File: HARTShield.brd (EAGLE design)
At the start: 61.9 x 66 mm, 31 parts, among them Y1 3M6864

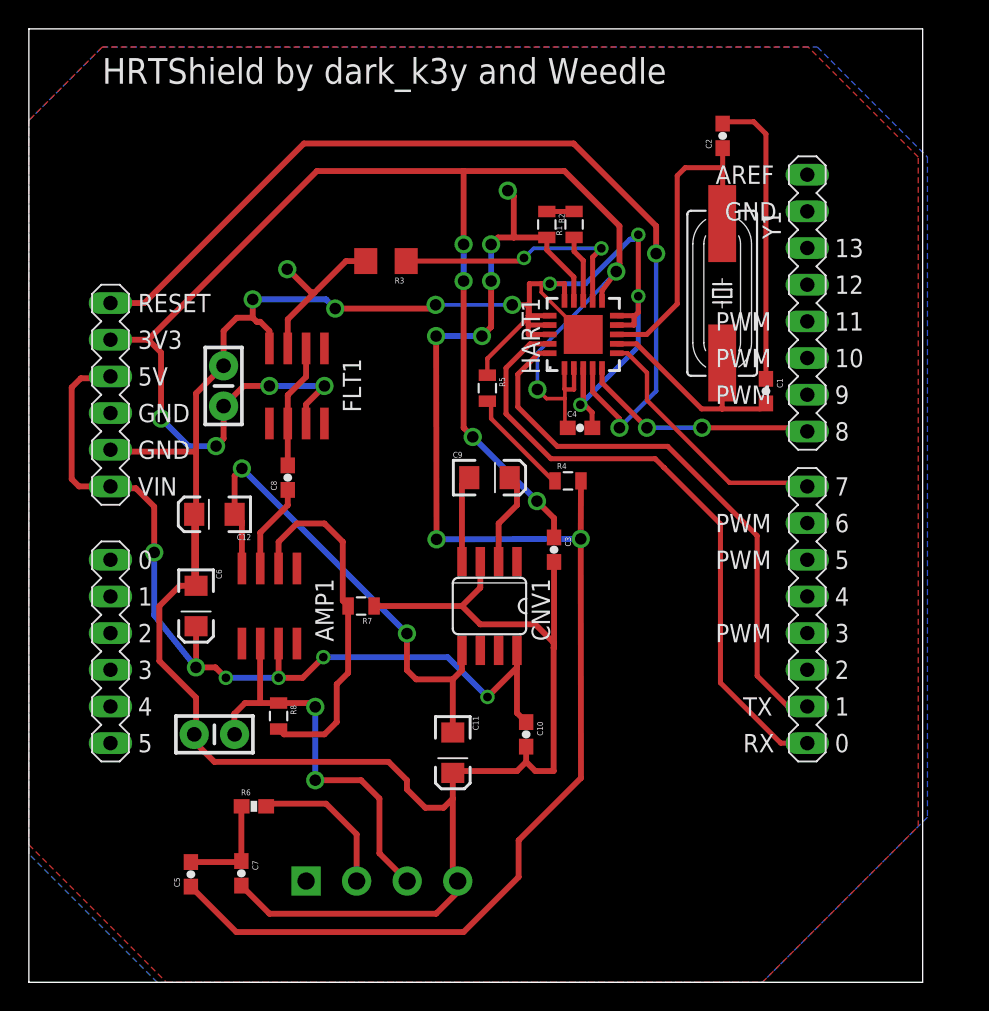
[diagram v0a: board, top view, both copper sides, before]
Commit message: Minor fixes on partlist.
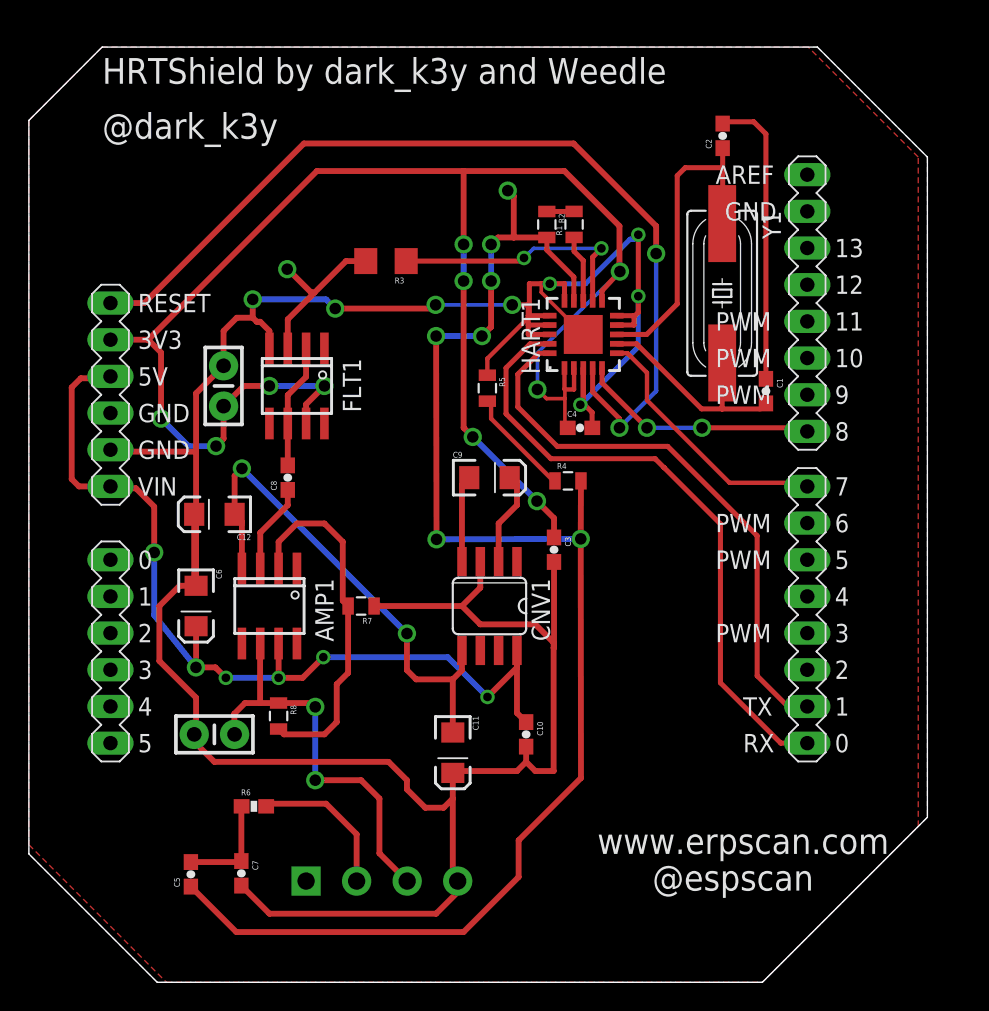
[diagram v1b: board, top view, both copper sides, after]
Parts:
- AMP1: value OP177GS -> OP37GS
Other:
- board size 61.9 x 66 mm -> 62.2 x 64.8 mm
- board text added: "@dark_k3y"
- board text added: "@espscan"
- board text added: "www.erpscan.com"
- board text removed: "GND"
- board text removed: "HI"
- board text removed: "HO"
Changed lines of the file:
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@@
 <layer number="25" name="tNames" color="7" fill="1" visible="yes" active="yes"/>
 <layer number="26" name="bNames" color="7" fill="1" visible="yes" active="yes"/>
-<layer number="27" name="tValues" color="7" fill="1" visible="no" active="yes"/>
-<layer number="28" name="bValues" color="7" fill="1" visible="no" active="yes"/>
+<layer number="27" name="tValues" color="7" fill="1" visible="yes" active="yes"/>
+<layer number="28" name="bValues" color="7" fill="1" visible="yes" active="yes"/>
 <layer number="29" name="tStop" color="7" fill="3" visible="no" active="yes"/>
 <layer number="30" name="bStop" color="7" fill="6" visible="no" active="yes"/>
@@
 <board>
 <plain>
-<wire x1="21.59" y1="6.35" x2="83.49" y2="6.35" width="0" layer="20"/>
-<wire x1="83.49" y1="6.35" x2="83.49" y2="72.38" width="0" layer="20"/>
-<wire x1="83.49" y1="72.38" x2="21.59" y2="72.38" width="0" layer="20"/>
-<wire x1="21.59" y1="72.38" x2="21.59" y2="6.35" width="0" layer="20"/>
+<wire x1="30.48" y1="6.35" x2="72.39" y2="6.35" width="0" layer="20"/>
+<wire x1="72.39" y1="6.35" x2="83.82" y2="17.78" width="0" layer="20"/>
+<wire x1="83.82" y1="17.78" x2="83.82" y2="63.5" width="0" layer="20"/>
+<wire x1="83.82" y1="63.5" x2="76.2" y2="71.12" width="0" layer="20"/>
+<wire x1="26.67" y1="71.12" x2="76.2" y2="71.12" width="0" layer="20"/>
+<wire x1="21.59" y1="66.04" x2="21.59" y2="15.24" width="0" layer="20"/>
+<wire x1="21.59" y1="15.24" x2="30.48" y2="6.35" width="0" layer="20"/>
 <circle x="27.241" y="35.612" radius="0.35" width="0.4" layer="116"/>
 <circle x="75.501" y="22.912" radius="0.35" width="0.4" layer="116"/>
@@
 <circle x="36.344" y="41.935" radius="0.3" width="0.3" layer="116"/>
 <text x="26.67" y="68.58" size="1.778" layer="25" font="vector" ratio="15">HRTShield by dark_k3y and Weedle</text>
-<text x="44.45" y="7.62" size="1.778" layer="26" font="vector" ratio="15" rot="MR0">HI</text>
-<text x="49.53" y="7.62" size="1.778" layer="26" font="vector" ratio="15" rot="MR0">HO</text>
-<text x="55.88" y="7.62" size="1.778" layer="26" font="vector" ratio="15" rot="MR0">GND</text>
+<text x="26.67" y="64.77" size="1.778" layer="25" ratio="15">@dark_k3y</text>
+<text x="64.77" y="12.7" size="1.778" layer="25" ratio="15">@espscan</text>
+<text x="60.96" y="15.24" size="1.778" layer="25" ratio="15">www.erpscan.com</text>
+<wire x1="26.66" y1="71.12" x2="21.59" y2="66.04" width="0" layer="20"/>
 </plain>
 <attributes>
@@
 </class>
 </classes>
-<designrules name="default">
-<description language="de">&lt;b&gt;EAGLE Design Rules&lt;/b&gt;
+<designrules name="DFRobot_Eagle_Rule_v0.4">
+<description language="en">
+&lt;b&gt;EAGLE Design Rules&lt;/b&gt;
 &lt;p&gt;
-Die Standard-Design-Rules sind so gewählt, dass sie für
-die meisten Anwendungen passen. Sollte ihre Platine
-besondere Anforderungen haben, treffen Sie die erforderlichen
-Einstellungen hier und speichern die Design Rules unter
-einem neuen Namen ab.</description>
-<description language="en">&lt;b&gt;EAGLE Design Rules&lt;/b&gt;
+The default Design Rules have been set to cover
+a wide range of applications. Your particular design
+may have different requirements, so please make the
+necessary adjustments and save your customized
+design rules under a new name.
+</description>
+<description language="it">
+&lt;b&gt;EAGLE Design Rules&lt;/b&gt;
 &lt;p&gt;
 The default Design Rules have been set to cover
@@
 <param name="mtCopper" value="0.035mm 0.035mm 0.035mm 0.035mm 0.035mm 0.035mm 0.035mm 0.035mm 0.035mm 0.035mm 0.035mm 0.035mm 0.035mm 0.035mm 0.035mm 0.035mm"/>
 <param name="mtIsolate" value="1.5mm 0.15mm 0.2mm 0.15mm 0.2mm 0.15mm 0.2mm 0.15mm 0.2mm 0.15mm 0.2mm 0.15mm 0.2mm 0.15mm 0.2mm"/>
-<param name="mdWireWire" value="8mil"/>
-<param name="mdWirePad" value="8mil"/>
-<param name="mdWireVia" value="8mil"/>
-<param name="mdPadPad" value="8mil"/>
-<param name="mdPadVia" value="8mil"/>
-<param name="mdViaVia" value="8mil"/>
-<param name="mdSmdPad" value="8mil"/>
-<param name="mdSmdVia" value="8mil"/>
-<param name="mdSmdSmd" value="8mil"/>
+<param name="mdWireWire" value="6mil"/>
+<param name="mdWirePad" value="6mil"/>
+<param name="mdWireVia" value="6mil"/>
+<param name="mdPadPad" value="6mil"/>
+<param name="mdPadVia" value="6mil"/>
+<param name="mdViaVia" value="6mil"/>
+<param name="mdSmdPad" value="0mil"/>
+<param name="mdSmdVia" value="0mil"/>
+<param name="mdSmdSmd" value="0mil"/>
 <param name="mdViaViaSameLayer" value="8mil"/>
 <param name="mnLayersViaInSmd" value="2"/>
-<param name="mdCopperDimension" value="40mil"/>
-<param name="mdDrill" value="8mil"/>
+<param name="mdCopperDimension" value="10mil"/>
+<param name="mdDrill" value="10mil"/>
 <param name="mdSmdStop" value="0mil"/>
-<param name="msWidth" value="10mil"/>
-<param name="msDrill" value="24mil"/>
-<param name="msMicroVia" value="9.99mm"/>
+<param name="msWidth" value="6mil"/>
+<param name="msDrill" value="12mil"/>
+<param name="msMicroVia" value="12mil"/>
 <param name="msBlindViaRatio" value="0.5"/>
 <param name="rvPadTop" value="0.25"/>
@@
 <param name="rvMicroViaOuter" value="0.25"/>
 <param name="rvMicroViaInner" value="0.25"/>
-<param name="rlMinPadTop" value="10mil"/>
+<param name="rlMinPadTop" value="12mil"/>
 <param name="rlMaxPadTop" value="20mil"/>
 <param name="rlMinPadInner" value="10mil"/>
 <param name="rlMaxPadInner" value="20mil"/>
-<param name="rlMinPadBottom" value="10mil"/>
+<param name="rlMinPadBottom" value="12mil"/>
 <param name="rlMaxPadBottom" value="20mil"/>
 <param name="rlMinViaOuter" value="8mil"/>
@@
 <param name="mvStopFrame" value="1"/>
 <param name="mvCreamFrame" value="0"/>
-<param name="mlMinStopFrame" value="4mil"/>
-<param name="mlMaxStopFrame" value="4mil"/>
+<param name="mlMinStopFrame" value="2mil"/>
+<param name="mlMaxStopFrame" value="2mil"/>
 <param name="mlMinCreamFrame" value="0mil"/>
 <param name="mlMaxCreamFrame" value="0mil"/>
-<param name="mlViaStopLimit" value="0mil"/>
+<param name="mlViaStopLimit" value="25mil"/>
 <param name="srRoundness" value="0"/>
 <param name="srMinRoundness" value="0mil"/>
@@
 <attribute name="PROD_ID" value="CAP-00811" x="-17.63075625" y="5.7395625" size="1.778" layer="27" rot="R270" display="off"/>
 </element>
-<element name="AMP1" library="hartmodems" package="SO8" value="OP177GS" x="38.24924375" y="32.4095625" rot="R180"/>
+<element name="AMP1" library="hartmodems" package="SO8" value="OP37GS" x="38.24924375" y="32.4095625" rot="R180"/>
 <element name="HART1" library="hartmodems" package="TQFN20-5X5" value="DS8500TQFN20" x="59.9840875" y="51.216696875" rot="R90"/>
 <element name="C8" library="SparkFun-Capacitors" package="0603-CAP" value="4.7uF" x="39.51924375" y="41.2995625" rot="R90">
@@
 <via x="56.8090875" y="47.406696875" extent="1-16" drill="0.8" diameter="1.27"/>
 <wire x1="56.8090875" y1="47.406696875" x2="56.8090875" y2="49.946696875" width="0.254" layer="16"/>
-<wire x1="56.8090875" y1="49.946696875" x2="62.268825" y2="55.574759375" width="0.254" layer="16"/>
-<via x="62.268825" y="55.574759375" extent="1-16" drill="0.8" diameter="1.27"/>
+<wire x1="56.8090875" y1="49.946696875" x2="62.522825" y2="55.574759375" width="0.254" layer="16"/>
+<via x="62.522825" y="55.574759375" extent="1-16" drill="0.8" diameter="1.27"/>
 <wire x1="27.2405125" y1="50.852459375" x2="29.856396875" y2="50.852459375" width="0.4064" layer="1"/>
 <wire x1="29.856396875" y1="50.852459375" x2="41.538090625" y2="62.534153125" width="0.4064" layer="1"/>
@@
 <wire x1="58.683090625" y1="62.534153125" x2="62.493090625" y2="58.724153125" width="0.4064" layer="1"/>
 <wire x1="62.493090625" y1="58.724153125" x2="62.493090625" y2="56.117109375" width="0.4064" layer="1"/>
-<wire x1="62.493090625" y1="56.117109375" x2="62.268825" y2="55.574759375" width="0.4064" layer="1"/>
+<wire x1="62.493090625" y1="56.117109375" x2="62.522825" y2="55.574759375" width="0.4064" layer="1"/>
 <wire x1="29.856396875" y1="50.852459375" x2="30.743090625" y2="49.965765625" width="0.4064" layer="1"/>
 <wire x1="30.743090625" y1="49.965765625" x2="30.743090625" y2="45.389153125" width="0.4064" layer="1"/>
@@
 <wire x1="51.698090625" y1="57.454153125" x2="51.698090625" y2="62.534153125" width="0.4064" layer="1"/>
 <wire x1="61.2840875" y1="53.541696875" x2="61.2840875" y2="54.2378" width="0.35" layer="1"/>
-<wire x1="61.2840875" y1="54.2378" x2="62.268825" y2="55.574759375" width="0.35" layer="1"/>
+<wire x1="61.2840875" y1="54.2378" x2="62.522825" y2="55.574759375" width="0.35" layer="1"/>
 </signal>
 <signal name="RST">
